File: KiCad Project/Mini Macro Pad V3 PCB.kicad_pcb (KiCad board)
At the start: 4 copper layers, 65 x 65 mm, 97 parts, among them J1 USB_C_Receptacle_USB2.0_14P, SW1 SW_Push bootsel, SW10 SW_Push, SW11 SW_Push, SW12 SW_Push, SW13 SW_Push, SW14 SW_Push, SW15 SW_Push, SW16 SW_Push, SW17 SW_Push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

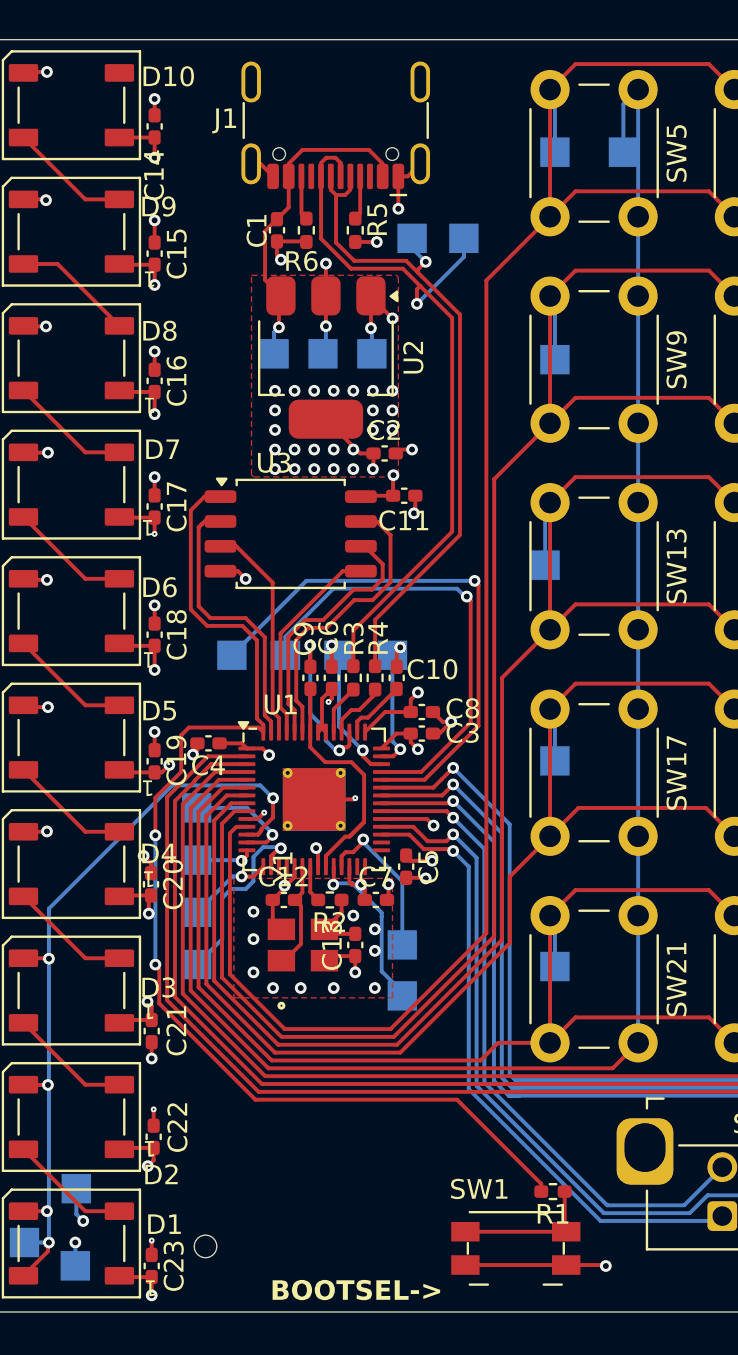
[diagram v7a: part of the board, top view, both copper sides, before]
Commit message: changed capacitor & resistor sizes
changed sizes from 0402 to 0603 & replaced BOOTSEL button with the same kind as all the others
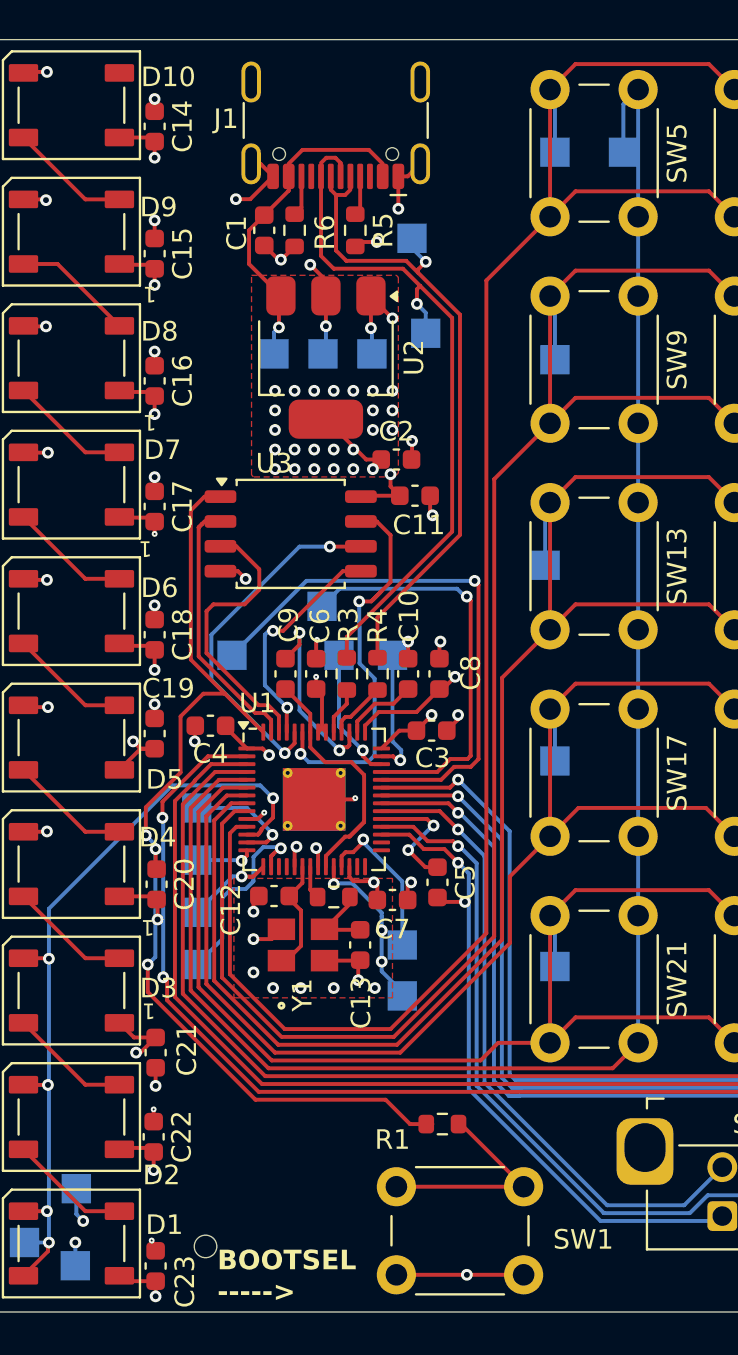
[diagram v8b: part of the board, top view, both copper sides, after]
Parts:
- C1, C10, C11, C12, C13, C14, C15, C16, C17, C18, C19, C2, C20, C21, C22, C23, C3, C4, C5, C6, C7, C8, C9: footprint Capacitor_SMD:C_0402_1005Metric_Pad0.74x0.62mm_HandSolder -> Capacitor_SMD:C_0603_1608Metric
- R1, R2, R3, R4, R5, R6: footprint Resistor_SMD:R_0402_1005Metric_Pad0.72x0.64mm_HandSolder -> Resistor_SMD:R_0603_1608Metric
- SW1: footprint Button_Switch_SMD:Panasonic_EVQPUK_EVQPUB -> Button_Switch_THT:SW_PUSH_6mm_H4.3mm
- moved R1 6.62 mm to (125.8, 112.7)
- moved TP8 5.23 mm to (124.9, 72.2)
- moved TP14 3.12 mm to (119.6, 86.2)
- moved C8 2.15 mm to (125.6, 89.7), turned to 90 degrees
- moved C5 1.79 mm to (125.5, 100.3)
- moved C19 1.42 mm to (111.0, 92.7)
- moved SW1 1.41 mm to (129.9, 120.3)
- moved C9 1.29 mm to (117.7, 89.7)
- moved C21 1.12 mm to (111.1, 109.0)
- moved C4 0.91 mm to (113.9, 92.3)
- moved C7 0.85 mm to (123.2, 101.2)
- moved C6 0.83 mm to (119.3, 89.7)
- moved C2 0.68 mm to (123.4, 78.7)
- moved C1 0.65 mm to (116.7, 67.0)
- moved C10 0.62 mm to (124.0, 89.7)
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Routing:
- net /QSPI_SS: track 58.2 -> 49.9 mm
- net +3.3V: track 61.8 -> 68.0 mm
- net /QSPI_SCLK: track 13.1 -> 18.4 mm, vias 0 -> 2
- net /QSPI_SD3: track 15.1 -> 20.2 mm, vias 0 -> 2
- net Net-(R1-Pad1): track 7.12 -> 11.2 mm
- net /QSPI_SD2: track 11.2 -> 14.7 mm
- net GND: track 58.6 -> 61.3 mm, vias 48 -> 49
- net Net-(U1-GPIO27_ADC1): track 23.5 -> 21.1 mm
- net /USB_D+: track 38.7 -> 36.2 mm
- net Net-(U1-VREG_VOUT): track 8.47 -> 9.77 mm
- net /QSPI_SD0: track 10.6 -> 11.7 mm, vias 0 -> 2
- net Net-(U1-GPIO26_ADC0): track 27.6 -> 28.6 mm
- net /QSPI_SD1: track 14.5 -> 13.8 mm
- net /USB_D-: track 34.2 -> 33.4 mm
- net /ENCODER_2_S1: track 51.7 -> 51.0 mm
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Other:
- board text added: "<3"
- board text added: "BOOTSEL ----->"
- board text removed: "BOOTSEL->"
